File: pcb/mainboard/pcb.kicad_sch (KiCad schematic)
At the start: 0 parts

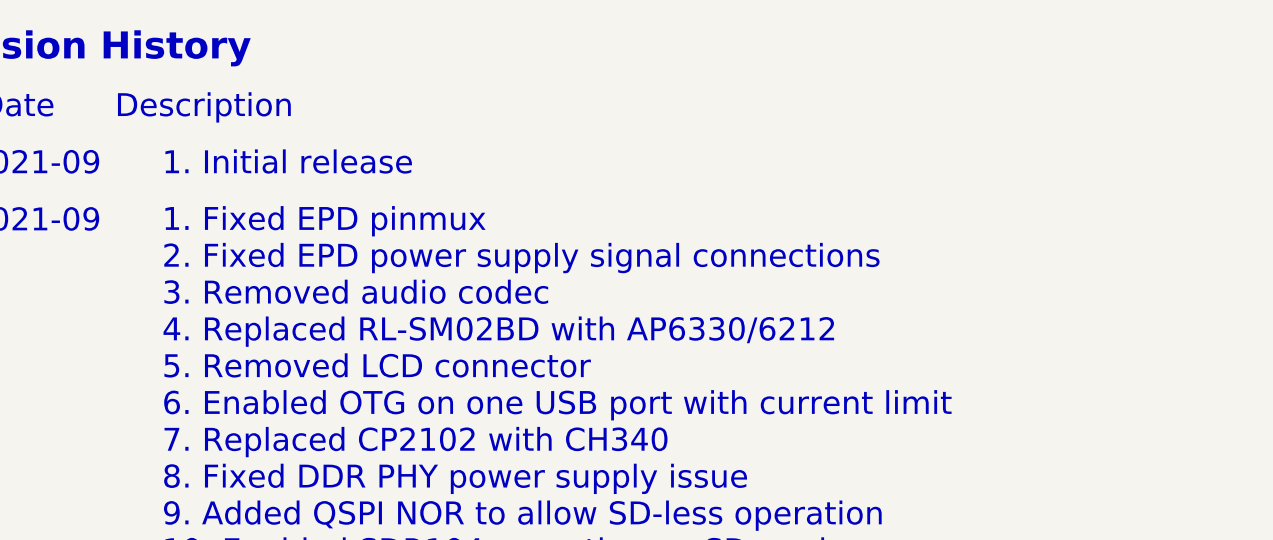
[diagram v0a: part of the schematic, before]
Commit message: pcb: switch to max17135, length tuning for QSPI and SD
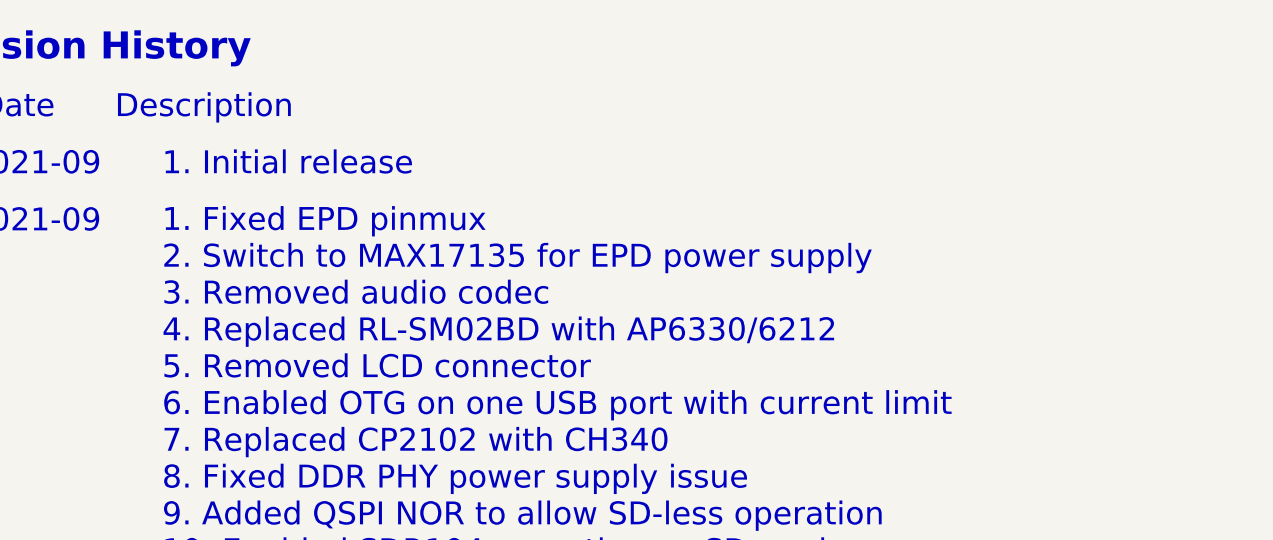
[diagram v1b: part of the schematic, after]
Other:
- note added: "1. Fixed EPD pinmux 2. Switch to MAX17135 for EPD power supply 3. Removed audio codec 4. Replaced RL-SM02BD with AP6330/6212 5. Removed LCD connector 6. Enabled OTG on one USB port with current limit 7. Replaced CP2102 with CH340 8. Fixed DDR PHY power supply issue 9. Added QSPI NOR to allow SD-less operation 10. Enabled SDR104 operation on SD card 11. Added additional DDR clock termination 12. A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"
- note removed: "1. Fixed EPD pinmux 2. Fixed EPD power supply signal connections 3. Removed audio codec 4. Replaced RL-SM02BD with AP6330/6212 5. Removed LCD connector 6. Enabled OTG on one USB port with current limit 7. Replaced CP2102 with CH340 8. Fixed DDR PHY power supply issue 9. Added QSPI NOR to allow SD-less operation 10. Enabled SDR104 operation on SD card 11. Added additional DDR clock termination 12.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"
